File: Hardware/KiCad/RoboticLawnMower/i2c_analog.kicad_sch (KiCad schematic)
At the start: 6 parts, among them U8 ADS1115IDGS, U9 ADS1115IDGS

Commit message: Layout
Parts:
- added C26, C27, C28, C29, C30, C31, C32, C33: 10n, Capacitor_SMD:C_0603_1608Metric, symbol Device:C
- added J14, J15: Conn_01x06, Connector_JST:JST_XA_B06B-XASK-1-A_1x06_P2.50mm_Vertical, symbol Connector_Generic:Conn_01x06
- added R43, R44, R45, R46, R47, R48, R49, R50: 1k, Resistor_SMD:R_0603_1608Metric, symbol Device:R
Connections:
- net +3.3V: now also U9.1 (ADDR), J14.1 (Pin_1), J15.1 (Pin_1)
- net GND: now also U8.1 (ADDR), C26.2, C27.2, C28.2, C29.2, C30.2, C31.2, C32.2, C33.2, J14.6 (Pin_6), J15.6 (Pin_6)
- net at U8.4 (AIN0): now also C32.1, R43.1
- net at U8.5 (AIN1): now also C30.1, R44.1
- net at U8.6 (AIN2): now also C28.1, R45.1
- net at U8.7 (AIN3): now also C26.1, R46.1
- net at U9.4 (AIN0): now also C33.1, R47.1
- net at U9.5 (AIN1): now also C31.1, R48.1
- net at U9.6 (AIN2): now also C29.1, R49.1
- net at U9.7 (AIN3): now also C27.1, R50.1
- new net: J15.2 (Pin_2), R47.2
- new net: J15.3 (Pin_3), R48.2
- new net: J15.4 (Pin_4), R49.2
- new net: J15.5 (Pin_5), R50.2
- new net: J14.3 (Pin_3), R44.2
- new net: J14.4 (Pin_4), R45.2
- new net: J14.2 (Pin_2), R43.2
- new net: J14.5 (Pin_5), R46.2
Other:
- moved on the sheet: U9

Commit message: Layout
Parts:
- J14, J15: footprint Connector_JST:JST_XA_B06B-XASK-1-A_1x06_P2.50mm_Vertical -> Connector_JST:JST_XA_B06B-XASK-1_1x06_P2.50mm_Vertical
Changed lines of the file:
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@@
       (effects (font (size 1.27 1.27)) (justify left))
     )
-    (property "Footprint" "Connector_JST:JST_XA_B06B-XASK-1-A_1x06_P2.50mm_Vertical" (id 2) (at 217.17 124.46 0)
+    (property "Footprint" "Connector_JST:JST_XA_B06B-XASK-1_1x06_P2.50mm_Vertical" (id 2) (at 217.17 124.46 0)
       (effects (font (size 1.27 1.27)) hide)
     )
@@
       (effects (font (size 1.27 1.27)) (justify left))
     )
-    (property "Footprint" "Connector_JST:JST_XA_B06B-XASK-1-A_1x06_P2.50mm_Vertical" (id 2) (at 217.17 73.66 0)
-      (effects (font (size 1.27 1.27)) hide)
-    )
+    (property "Footprint" "Connector_JST:JST_XA_B06B-XASK-1_1x06_P2.50mm_Vertical" (id 2) (at 217.17 73.66 0)
+      (effects (font (size 1.27 1.27)) hide)
+    )

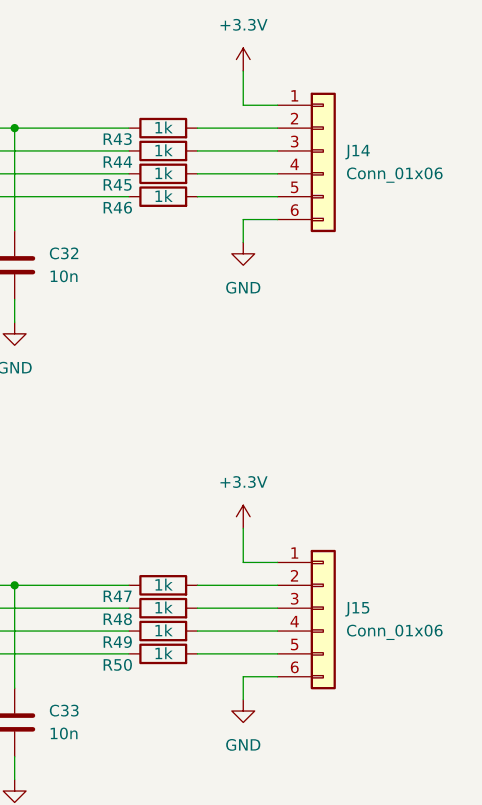
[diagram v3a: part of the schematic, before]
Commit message: Schaltplan & Layout Änderung
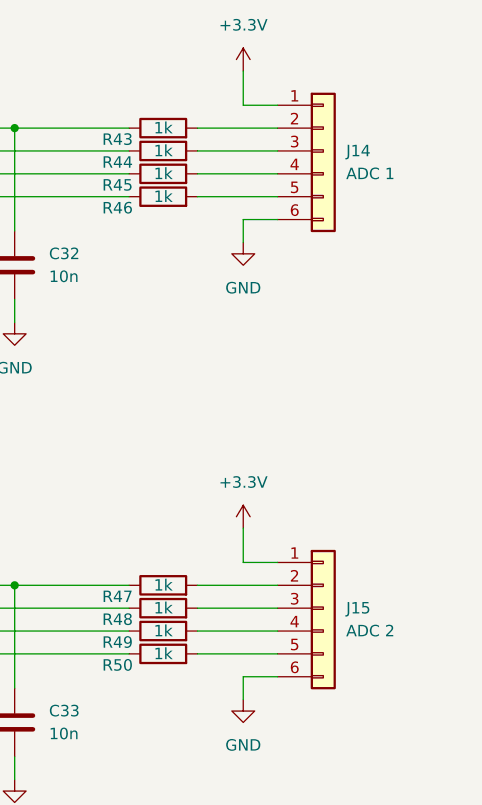
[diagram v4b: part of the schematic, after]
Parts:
- J14: value Conn_01x06 -> ADC 1
- J15: value Conn_01x06 -> ADC 2
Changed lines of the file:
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@@
       (effects (font (size 1.27 1.27)) (justify left))
     )
-    (property "Value" "Conn_01x06" (id 1) (at 219.71 126.9999 0)
+    (property "Value" "ADC 2" (id 1) (at 219.71 126.9999 0)
       (effects (font (size 1.27 1.27)) (justify left))
     )
@@
       (effects (font (size 1.27 1.27)) (justify left))
     )
-    (property "Value" "Conn_01x06" (id 1) (at 219.71 76.1999 0)
-      (effects (font (size 1.27 1.27)) (justify left))
-    )
+    (property "Value" "ADC 1" (id 1) (at 219.71 76.1999 0)
+      (effects (font (size 1.27 1.27)) (justify left))
+    )
